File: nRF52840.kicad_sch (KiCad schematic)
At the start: 55 parts, among them J1 MM8130-2600RA2, J2 2X05, SW1 PTS840_GK_SMTR_LFS, U4 NRF52840, U8 BME280, Y2 ABM11W-101-32.0000MHZ-T3, Y3 ABS06-32.768KHZ-9-1-T

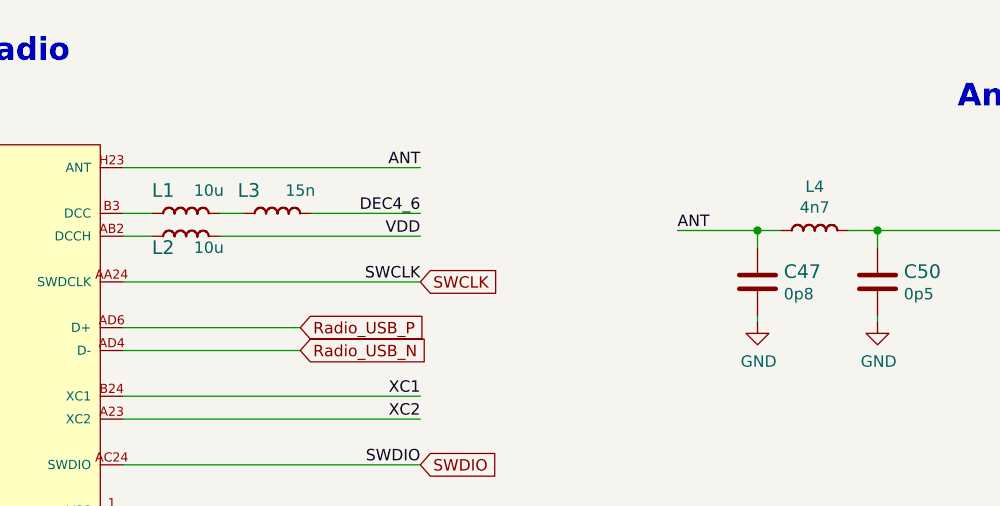
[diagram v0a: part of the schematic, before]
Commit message: [#102286] Bump to KiCad10
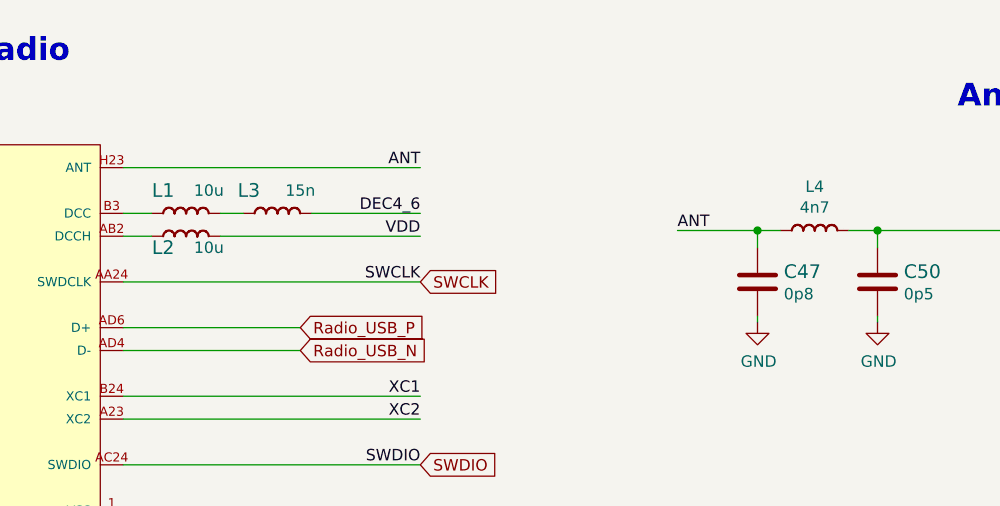
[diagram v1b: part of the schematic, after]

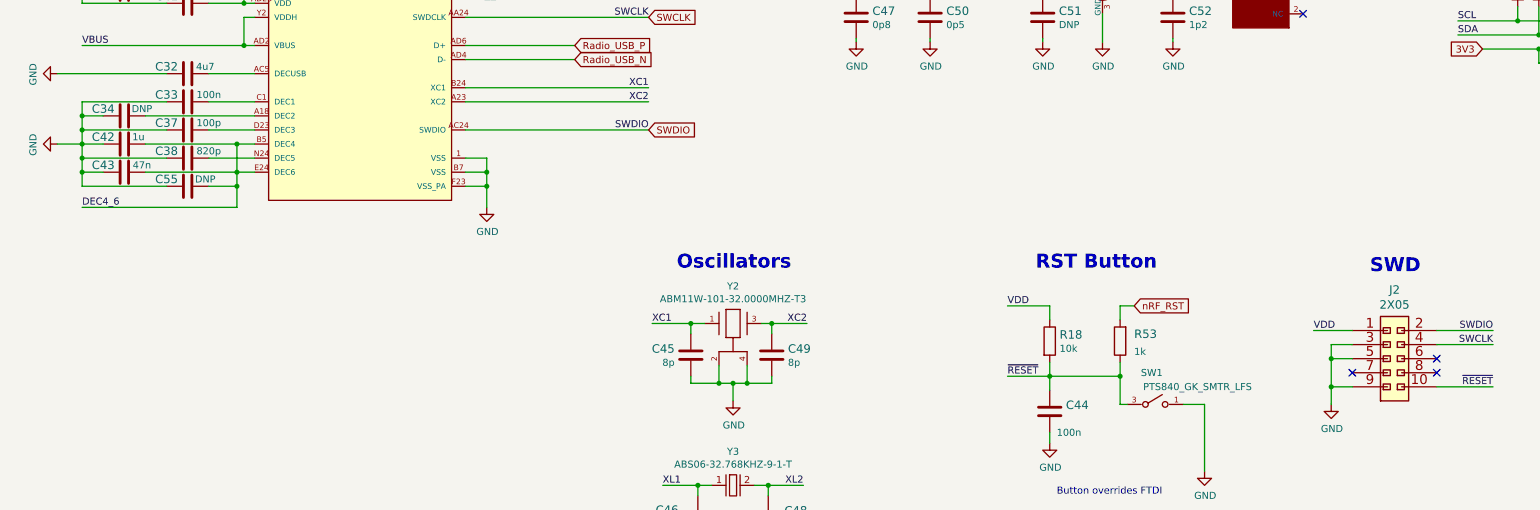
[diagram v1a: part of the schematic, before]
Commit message: [#102286] Fix legacy DNP
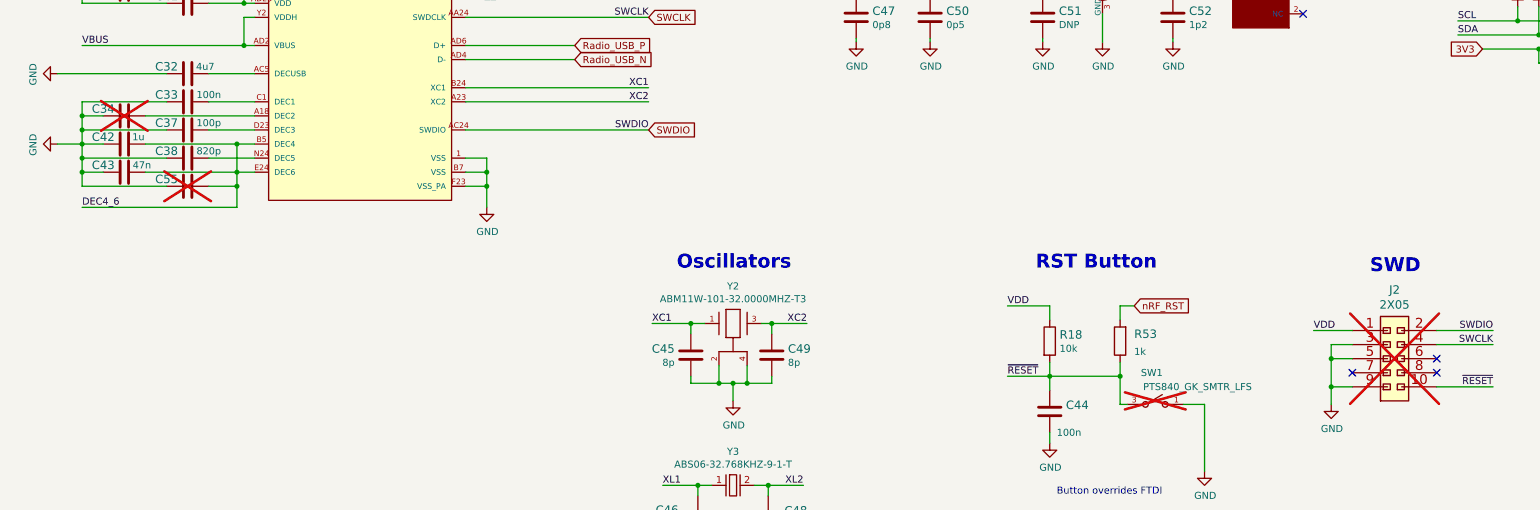
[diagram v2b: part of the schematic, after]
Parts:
- C34, C55, J2, SW1: DNP DNP -> (none); now not fitted
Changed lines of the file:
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@@
 		(on_board yes)
 		(in_pos_files yes)
-		(dnp no)
+		(dnp yes)
 		(property "Reference" "C34"
 			(at 62.865 82.55 90)
@@
 			)
 		)
-		(property "DNP" "DNP"
-			(at 69.85 82.55 90)
-			(show_name no)
-			(do_not_autoplace no)
-			(effects
-				(font
-					(size 1.27 1.27)
-				)
-			)
-		)
 		(pin "1"
 		)
@@
 		(on_board yes)
 		(in_pos_files yes)
-		(dnp no)
+		(dnp yes)
 		(property "Reference" "SW1"
 			(at 252.095 130.175 0)
@@
 			)
 		)
-		(property "DNP" "DNP"
-			(at 247.65 130.81 0)
-			(hide yes)
-			(show_name no)
-			(do_not_autoplace no)
-			(effects
-				(font
-					(size 1.27 1.27)
-				)
-			)
-		)
 		(pin "1"
 		)
@@
 		(on_board yes)
 		(in_pos_files yes)
-		(dnp no)
+		(dnp yes)
 		(property "Reference" "J2"
 			(at 295.91 115.2144 0)
@@
 			)
 		)
-		(property "DNP" "DNP"
-			(at 295.91 122.555 0)
-			(hide yes)
-			(show_name no)
-			(do_not_autoplace no)
-			(effects
-				(font
-					(size 1.27 1.27)
-				)
-			)
-		)
 		(pin "1"
 		)
@@
 		(on_board yes)
 		(in_pos_files yes)
-		(dnp no)
+		(dnp yes)
 		(property "Reference" "C55"
 			(at 74.295 95.25 90)
@@
 			(show_name no)
 			(do_not_autoplace no)
-			(effects
-				(font
-					(size 1.27 1.27)
-				)
-			)
-		)
-		(property "DNP" "DNP"
-			(at 81.28 95.25 90)
-			(show_name no)
-			(do_not_autoplace no)

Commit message: [#102286] Unify C_100n_0402 capacitors to use single MPN
Refs: C1, C3, C6, C7, C10, C13, C17, C18, C25-C29, C33, C36, C39, C41,
C44, C67-C71

Change from 0402X104K6R3CT to GRM155R61H104KE14D (same but limit 50V
instead of 6V3)
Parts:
- C33, C36, C39, C41, C44, C70, C71: MPN 0402X104K6R3CT -> GRM155R61H104KE14D; Manufacturer Walsin -> Murata
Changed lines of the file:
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@@
 		)
 		(property "Intersheetrefs" "${INTERSHEET_REFS}"
-			(at 0 0 0)
+			(at 39.7907 196.85 0)
 			(hide yes)
 			(show_name no)
@@
 					(size 1.27 1.27)
 				)
+				(justify right)
 			)
 		)
@@
 		)
 		(property "Intersheetrefs" "${INTERSHEET_REFS}"
-			(at 0 0 0)
+			(at 358.6514 55.245 0)
 			(hide yes)
 			(show_name no)
@@
 					(size 1.27 1.27)
 				)
+				(justify right)
 			)
 		)
@@
 		)
 		(property "Intersheetrefs" "${INTERSHEET_REFS}"
-			(at 0 0 0)
+			(at 144.692 250.19 0)
 			(hide yes)
 			(show_name no)
@@
 					(size 1.27 1.27)
 				)
+				(justify left)
 			)
 		)
@@
 		)
 		(property "Intersheetrefs" "${INTERSHEET_REFS}"
-			(at 0 0 0)
+			(at 144.2081 204.47 0)
 			(hide yes)
 			(show_name no)
@@
 					(size 1.27 1.27)
 				)
+				(justify left)
 			)
 		)
@@
 		)
 		(property "Intersheetrefs" "${INTERSHEET_REFS}"
-			(at 0 0 0)
+			(at 162.623 71.12 0)
 			(hide yes)
 			(show_name no)
@@
 					(size 1.27 1.27)
 				)
+				(justify left)
 			)
 		)
@@
 		)
 		(property "Intersheetrefs" "${INTERSHEET_REFS}"
-			(at 0 0 0)
+			(at 349.3736 55.245 0)
 			(hide yes)
 			(show_name no)
@@
 					(size 1.27 1.27)
 				)
+				(justify left)
 			)
 		)
@@
 		)
 		(property "Intersheetrefs" "${INTERSHEET_REFS}"
-			(at 0 0 0)
+			(at 162.6835 73.66 0)
 			(hide yes)
 			(show_name no)
@@
 					(size 1.27 1.27)
 				)
+				(justify left)
 			)
 		)
@@
 		)
 		(property "Intersheetrefs" "${INTERSHEET_REFS}"
-			(at 0 0 0)
+			(at 305.3114 55.245 0)
 			(hide yes)
 			(show_name no)
@@
 					(size 1.27 1.27)
 				)
+				(justify right)
 			)
 		)
@@
 		)
 		(property "Intersheetrefs" "${INTERSHEET_REFS}"
-			(at 0 0 0)
+			(at 12.3344 48.895 0)
 			(hide yes)
 			(show_name no)
@@
 					(size 1.27 1.27)
 				)
+				(justify right)
 			)
 		)
@@
 		)
 		(property "Intersheetrefs" "${INTERSHEET_REFS}"
-			(at 0 0 0)
+			(at 305.9464 71.755 0)
 			(hide yes)
 			(show_name no)
@@
 					(size 1.27 1.27)
 				)
+				(justify right)
 			)
 		)
@@
 			)
 		)
-		(property "Manufacturer" "Walsin"
+		(property "Manufacturer" "Murata"
 			(at 76.835 66.04 0)
 			(hide yes)
@@
 			)
 		)
-		(property "MPN" "0402X104K6R3CT"
+		(property "MPN" "GRM155R61H104KE14D"
 			(at 74.295 66.04 0)
 			(hide yes)
@@
 			)
 		)
-		(property "Manufacturer" "Walsin"
+		(property "Manufacturer" "Murata"
 			(at 88.265 58.42 0)
 			(hide yes)
@@
 			)
 		)
-		(property "MPN" "0402X104K6R3CT"
+		(property "MPN" "GRM155R61H104KE14D"
 			(at 85.725 58.42 0)
 			(hide yes)
@@
 			)
 		)
-		(property "Manufacturer" "Walsin"
+		(property "Manufacturer" "Murata"
 			(at 88.265 68.58 0)
 			(hide yes)
@@
 			)
 		)
-		(property "MPN" "0402X104K6R3CT"
+		(property "MPN" "GRM155R61H104KE14D"
 			(at 85.725 68.58 0)
 			(hide yes)
@@
 			)
 		)
-		(property "Manufacturer" "Walsin"
+		(property "Manufacturer" "Murata"
 			(at 88.265 86.36 0)
 			(hide yes)
@@
 			)
 		)
-		(property "MPN" "0402X104K6R3CT"
+		(property "MPN" "GRM155R61H104KE14D"
 			(at 85.725 86.36 0)
 			(hide yes)
@@
 			)
 		)
-		(property "Manufacturer" "Walsin"
+		(property "Manufacturer" "Murata"
 			(at 238.76 127 0)
 			(hide yes)
@@
 			)
 		)
-		(property "MPN" "0402X104K6R3CT"
+		(property "MPN" "GRM155R61H104KE14D"
 			(at 238.76 129.54 0)
 			(hide yes)
@@
 			)
 		)
-		(property "Manufacturer" "Walsin"
+		(property "Manufacturer" "Murata"
 			(at 378.46 51.435 0)
 			(hide yes)
@@
 			)
 		)
-		(property "MPN" "0402X104K6R3CT"
+		(property "MPN" "GRM155R61H104KE14D"
 			(at 378.46 53.975 0)
 			(hide yes)
@@
 			)
 		)
-		(property "Manufacturer" "Walsin"
+		(property "Manufacturer" "Murata"
 			(at 361.95 71.755 0)
 			(hide yes)
@@
 			)
 		)
-		(property "MPN" "0402X104K6R3CT"
+		(property "MPN" "GRM155R61H104KE14D"
 			(at 361.95 69.215 0)
 			(hide yes)
